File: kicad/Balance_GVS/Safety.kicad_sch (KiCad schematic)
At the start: 35 parts, among them J1 Conn_01x02_Pin, J6 Conn_01x03_Pin, J7 Conn_01x03_Pin, J8 Conn_01x05_Pin, K1 AQY210S, Q3 2N3904, Q4 2N3904, SW2 EVQ-P7A01P, U3 OPA4313IPWR, U4 INA303A1IPW

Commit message: Fixed schematic warnings
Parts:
- removed D3: LED_Small, LED_SMD:LED_0603_1608Metric_Pad1.05x0.95mm_HandSolder, symbol Device:LED_Small
- added D3: LED, LED_SMD:LED_0603_1608Metric_Pad1.05x0.95mm_HandSolder, symbol Device:LED
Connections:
- net at K1.2 (K), Q4.3 (C): now also D3.1 (K)
- net at R6.2: now also D3.2 (A)

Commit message: I kinda popped off ngl. Main pcb almost done
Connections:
- net at D10.1 (A), D12.2 (C): now also J7.3 (Pin_3); no longer J7.1 (Pin_1)
- net at D15.2 (A): now also J7.1 (Pin_1); no longer J7.3 (Pin_3)
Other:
- moved on the sheet: J7
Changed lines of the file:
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@@
 	(wire
 		(pts
-			(xy 55.88 172.72) (xy 67.31 172.72)
+			(xy 62.23 172.72) (xy 67.31 172.72)
 		)
 		(stroke
@@
 		)
 	)
-	(label "VREF"
-		(at 55.88 172.72 0)
-		(effects
-			(font
-				(size 1.27 1.27)
-			)
-			(justify left bottom)
-		)
-	)
 	(label "INP"
 		(at 106.68 88.9 180)
@@
 		)
 	)
+	(label "1.65V"
+		(at 55.88 167.64 0)
+		(effects
+			(font
+				(size 1.27 1.27)
+			)
+			(justify left bottom)
+		)
+	)
 	(label "VREF"
 		(at 91.44 109.22 0)
@@
 		)
 	)
-	(global_label "1.65V"
+	(global_label "VREF"
 		(shape input)
-		(at 55.88 167.64 180)
+		(at 62.23 172.72 180)
 		(fields_autoplaced yes)
 		(effects
@@
 		)
 		(property "Intersheetrefs" "${INTERSHEET_REFS}"
-			(at 47.5729 167.64 0)
+			(at 54.6486 172.72 0)
 			(hide yes)
 			(show_name no)
@@
 	(symbol
 		(lib_id "Connector:Conn_01x03_Pin")
-		(at 269.24 81.28 90)
-		(mirror x)
+		(at 269.24 81.28 270)
 		(unit 1)
 		(body_style 1)
@@
 		(in_pos_files yes)
 		(dnp no)
-		(fields_autoplaced yes)
 		(property "Reference" "J7"
 			(at 269.24 76.2 90)

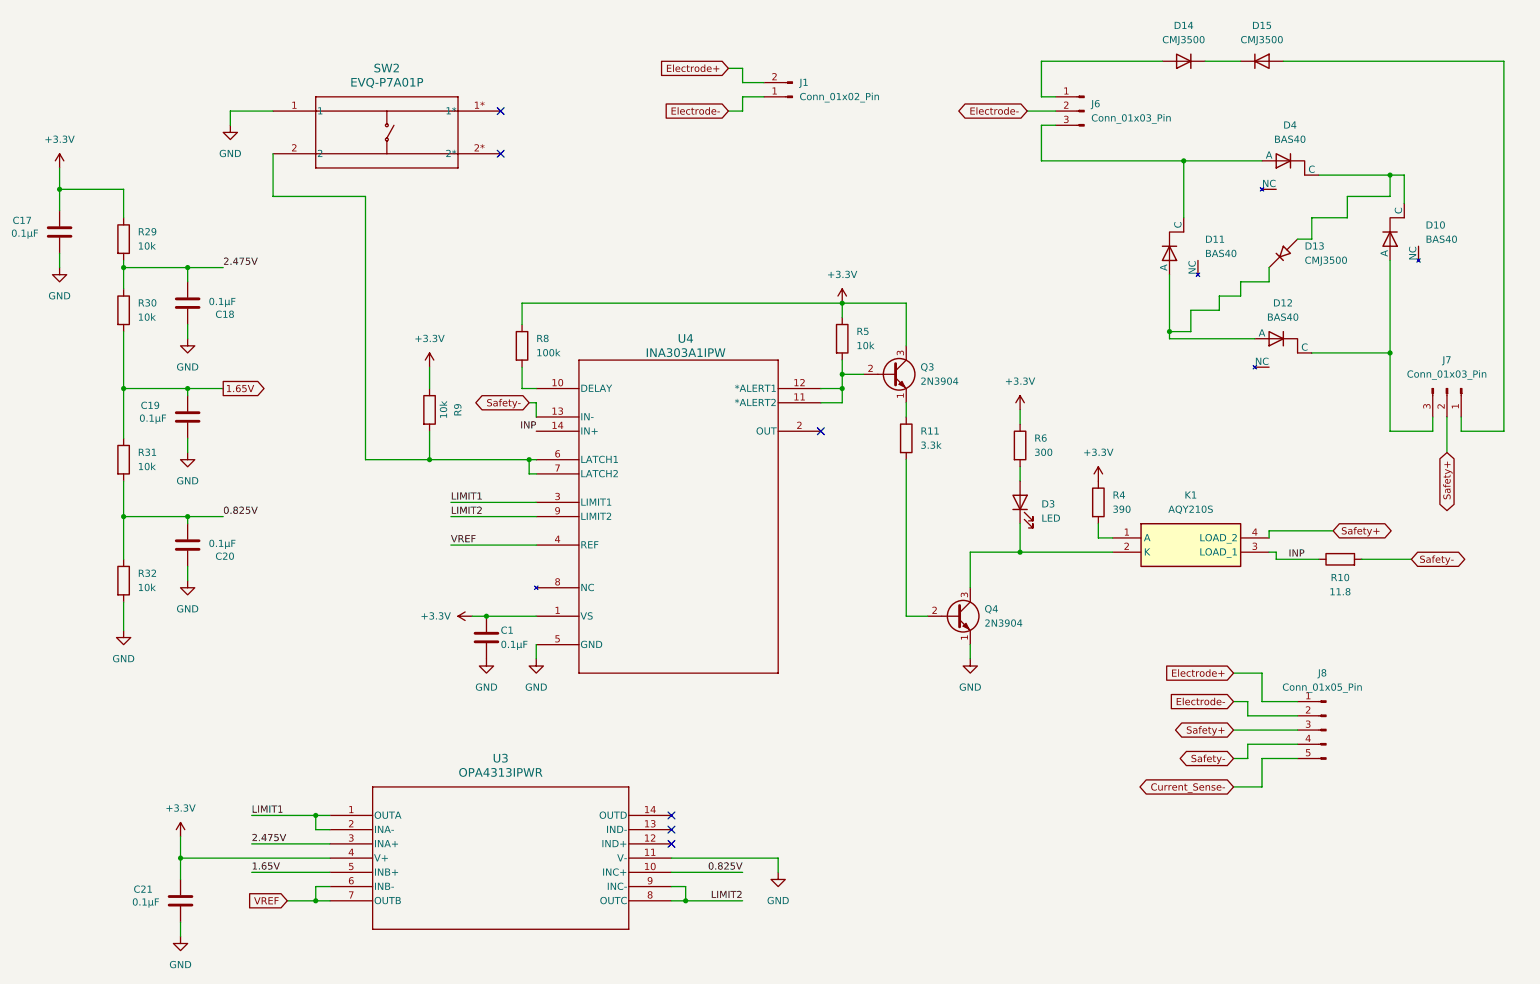
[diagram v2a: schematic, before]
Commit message: Add flip flop for better safety reset stability and remove NPNs
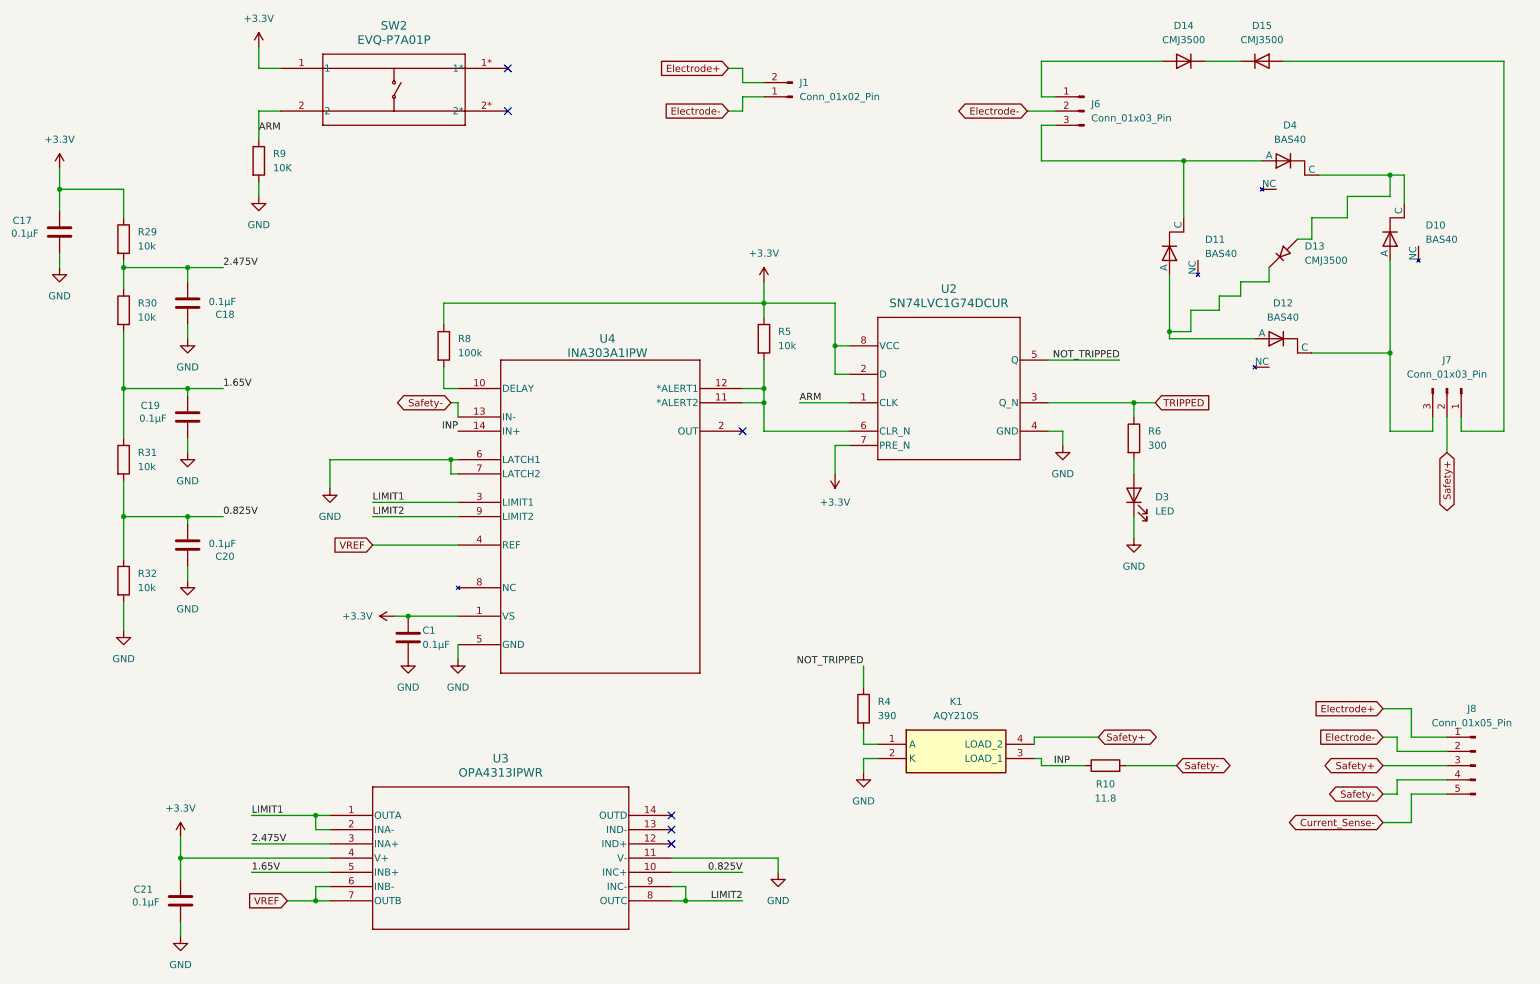
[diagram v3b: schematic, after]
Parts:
- removed Q3, Q4: 2N3904, Package_TO_SOT_THT:TO-92_Inline, symbol Transistor_BJT:2N3904
- removed R11: 3.3k, Resistor_SMD:R_0805_2012Metric_Pad1.20x1.40mm_HandSolder, symbol Device:R
- added U2: SN74LVC1G74DCUR, SN74LVC1G74DCUR:DCU0008A_M, symbol SN74LVC1G74DCUR:SN74LVC1G74DCUR
- R9: value 10k -> 10K
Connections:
- net +3.3V: now also SW2.1, U2.2 (D), U2.7 (PRE_N), U2.8 (VCC); no longer R4.1, R6.1, R9.1
- net GND: now also D3.1 (K), K1.2 (K), R9.2, U4.6 (LATCH1), U4.7 (LATCH2), U2.4 (GND); no longer SW2.1
- net at R5.2, U4.11 (*ALERT2), U4.12 (*ALERT1): now also U2.6 (CLR_N)
- new net ARM: R9.1, SW2.2, U2.1 (CLK)
- new net NOT_TRIPPED: R4.1, U2.5 (Q)
- new net TRIPPED: R6.1, U2.3 (Q_N)
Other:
- moved on the sheet: C1, D3, J8, K1, R10, R4, R5, R6, R8, SW2, U4

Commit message: Add flip flop changes to PCB
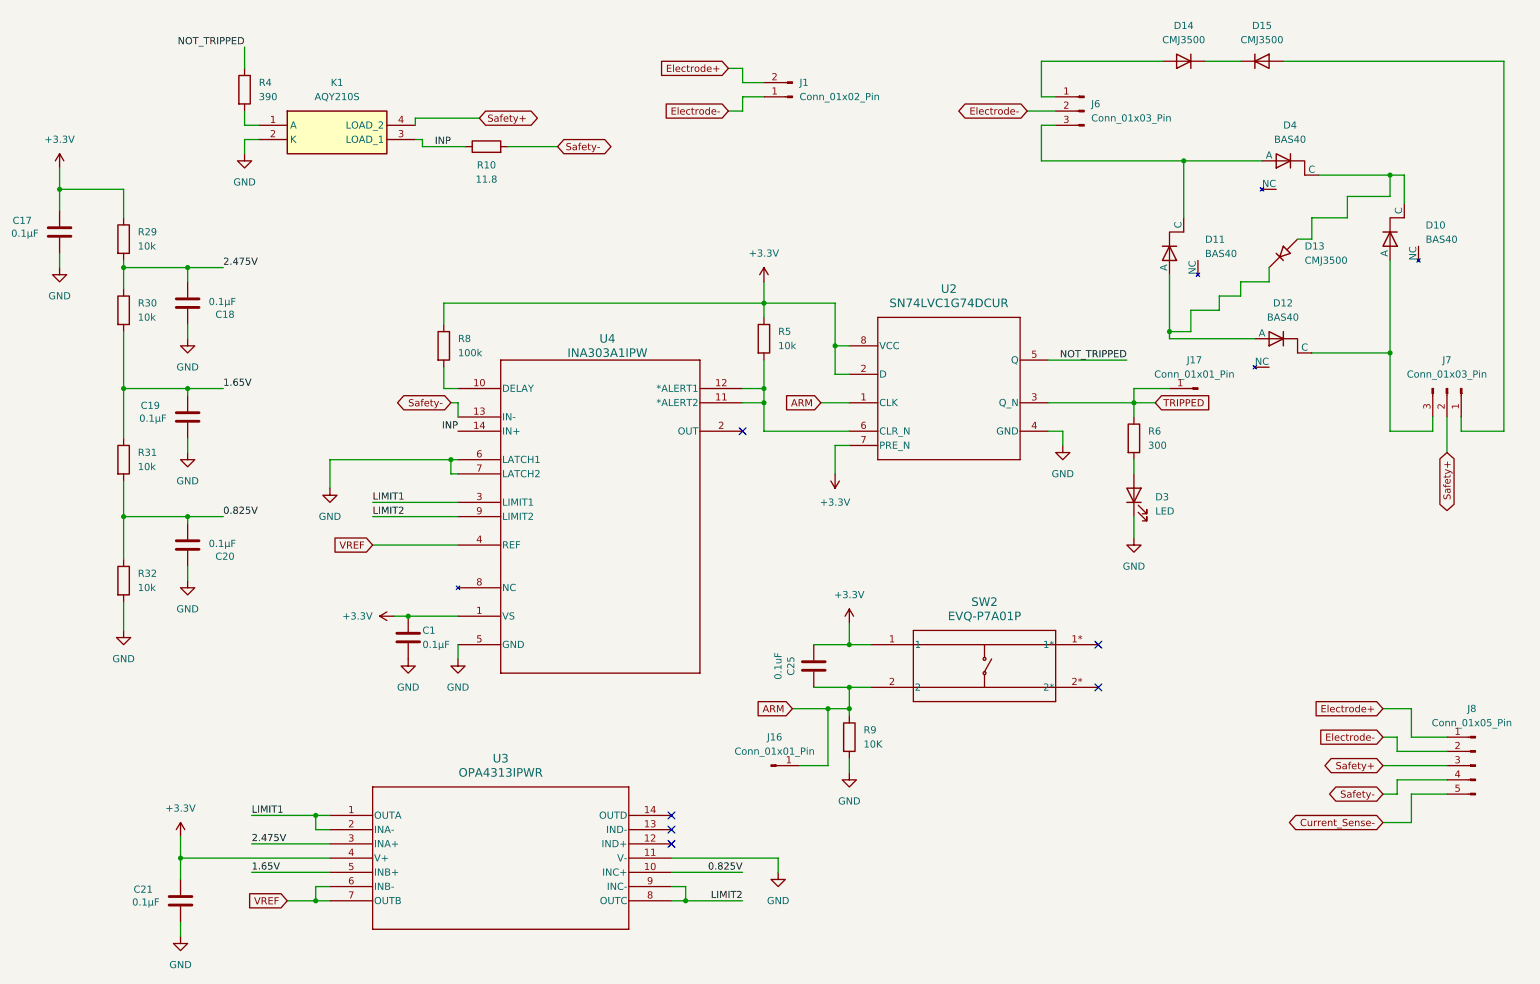
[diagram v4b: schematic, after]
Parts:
- added C25: 0.1uF, Capacitor_SMD:C_0805_2012Metric_Pad1.18x1.45mm_HandSolder, symbol Device:C
- added J16, J17: Conn_01x01_Pin, Connector_PinSocket_2.54mm:PinSocket_1x01_P2.54mm_Vertical, symbol Connector:Conn_01x01_Pin
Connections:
- net +3.3V: now also C25.1
- net ARM: now also C25.2, J16.1 (Pin_1)
- net TRIPPED: now also J17.1 (Pin_1)
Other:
- moved on the sheet: K1, R10, R4, R9, SW2

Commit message: Add Mark debug point testing and udpate silkscreen
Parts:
- removed J8: Conn_01x05_Pin, Connector_PinSocket_2.54mm:PinSocket_1x05_P2.54mm_Vertical, symbol Connector:Conn_01x05_Pin
- added J18, J19: Conn_01x03_Pin, Connector_PinHeader_2.54mm:PinHeader_1x03_P2.54mm_Vertical, symbol Connector:Conn_01x03_Pin
- added J2, J3: Conn_01x01_Pin, Connector_PinSocket_2.54mm:PinSocket_1x01_P2.54mm_Vertical, symbol Connector:Conn_01x01_Pin
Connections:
- net Electrode-: now also J18.2 (Pin_2); no longer J6.2 (Pin_2)
- net Safety+: now also J19.2 (Pin_2); no longer K1.4 (LOAD_2)
- new net: J19.3 (Pin_3), K1.4 (LOAD_2)
- new net: J18.3 (Pin_3), J6.2 (Pin_2)
- new net Electrode- TEST: J18.1 (Pin_1), J2.1 (Pin_1)
- new net Safety+ TEST: J19.1 (Pin_1), J3.1 (Pin_1)
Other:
- moved on the sheet: J1, K1, R10, R4
